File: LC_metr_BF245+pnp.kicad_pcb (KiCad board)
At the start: 2 copper layers, 37 x 33.5 mm, 16 parts, among them J1 Conn_01x01_Socket, J2 Conn_01x01_Socket, J3 Conn_02x01, J4 Conn_01x01_Socket, J5 Conn_01x01_Socket, Q1 MPSA92, Q2 BF245A, U2 LM317_TO-252

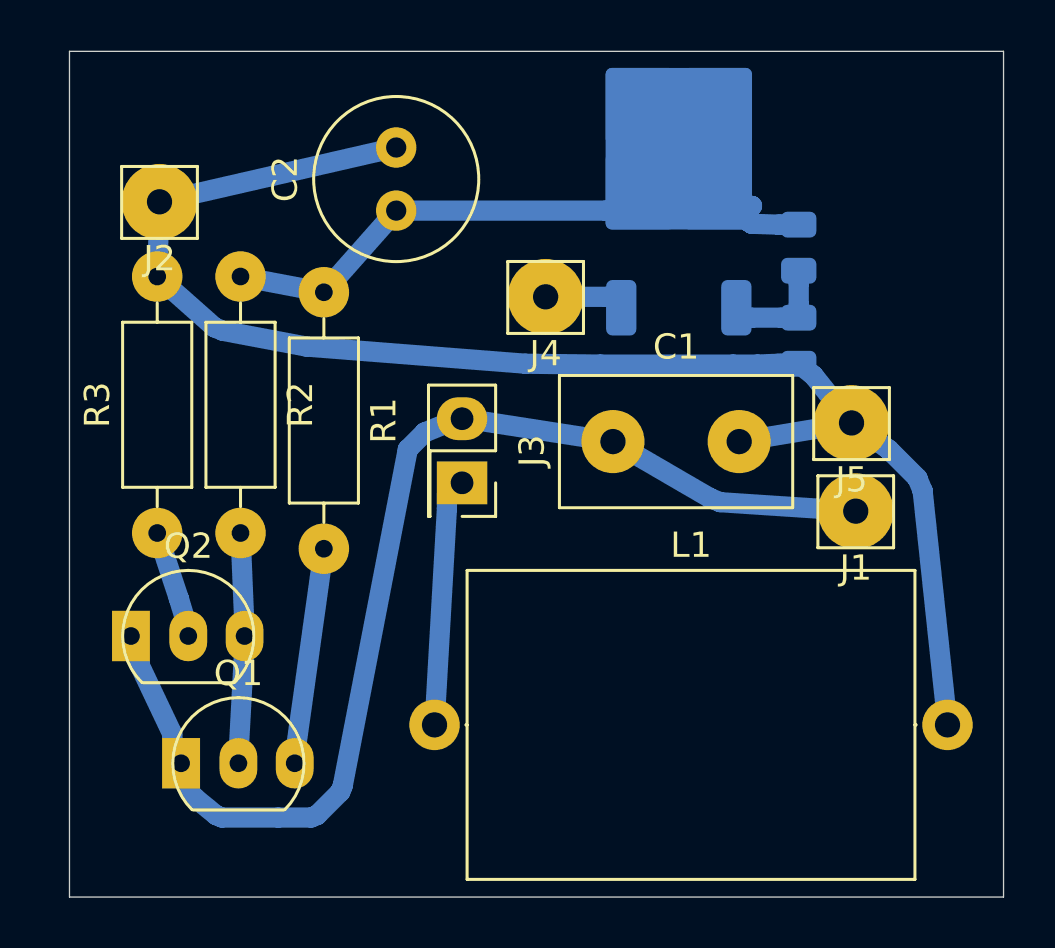
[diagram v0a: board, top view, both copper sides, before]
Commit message: оптимизация и доработка
добавлены выходные клемы, оптимизированно размещение элементов топором
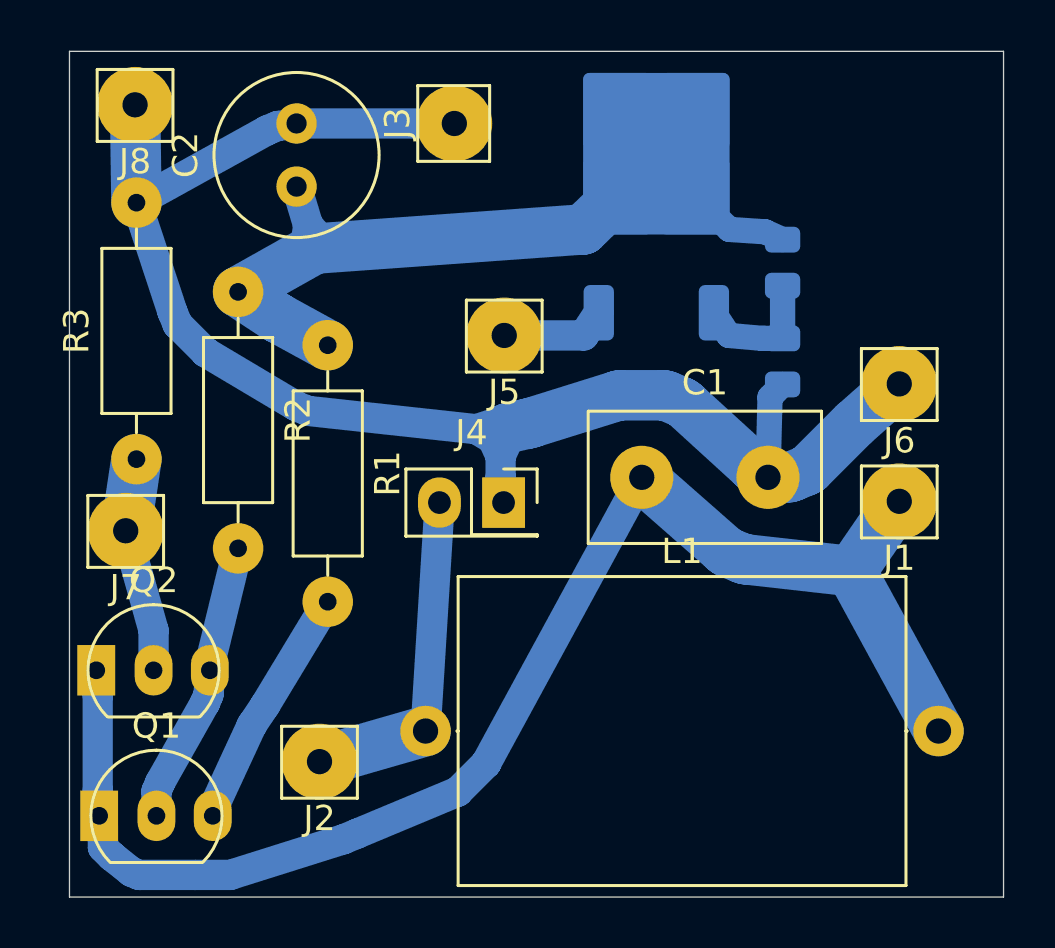
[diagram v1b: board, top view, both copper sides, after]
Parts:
- removed U2: LM317_TO-252, Package_TO_SOT_SMD:TO-252-2
- added J6: Conn_01x01_Socket, main:Pin_3mm_Dril_1mm, F.Cu at (59.9, 37.6)
- added J7: Conn_01x01_Socket, main:Pin_3mm_Dril_1mm, F.Cu at (29.3, 43.4)
- added J8: Conn_01x01_Socket, main:Pin_3mm_Dril_1mm, F.Cu at (29.6, 26.5)
- added U1: LM317_TO-252, Package_TO_SOT_SMD:TO-252-2, B.Cu at (50.3, 29.7)
- J3: value Conn_02x01 -> Conn_01x01_Socket; footprint main:PinSocket_2x01_P2.54mm_Vertical -> main:Pin_3mm_Dril_1mm
- J4: value Conn_01x01_Socket -> Conn_02x01; footprint main:Pin_3mm_Dril_1mm -> main:PinSocket_2x01_P2.54mm_Vertical
- moved J2 23.1 mm to (37.0, 52.5)
- moved J3 14.2 mm to (42.3, 27.2)
- moved J5 14.2 mm to (44.3, 35.6)
- moved J4 8.32 mm to (44.2, 42.3)
- moved C2 4.06 mm to (36.0, 29.8)
- moved Q1 3.86 mm to (29.2, 54.7)
- moved R3 3.04 mm to (29.7, 40.5)
- moved R1 2.10 mm to (37.3, 36.0)
- moved Q2 1.93 mm to (29.1, 48.9)
- moved C1 1.82 mm to (49.7, 41.3)
- moved J1 1.77 mm to (59.9, 42.2)
- moved R5 1.04 mm to (55.3, 36.7)
- moved R4 0.87 mm to (55.3, 32.8)
- moved R2 0.62 mm to (33.7, 33.9)
- moved L1 0.43 mm to (41.2, 51.3)
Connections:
- J2 pad 1: GND -> Net-(J2-Pin_1)
- J3 pad 1: Net-(J3-Pin_1) -> GND
- J4 pad 1: +12V -> GND
- J5 pad 1: GND -> +12V
- L1 pad 1: Net-(J3-Pin_1) -> Net-(J2-Pin_1)
- L1 pad 2: GND -> Net-(J1-Pin_1)
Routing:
- net Net-(J2-Pin_1): track 0.00 -> 13.4 mm
- net Net-(J1-Pin_1): track 46.2 -> 56.6 mm
- net Net-(J3-Pin_1): track 9.90 -> 0.00 mm
- net +5V: track 22.1 -> 28.6 mm
- net GND: track 59.8 -> 65.1 mm
- net Net-(J7-Pin_1): track 4.27 -> 8.55 mm
- net Net-(Q1-B): track 9.13 -> 11.3 mm
- net Net-(Q1-C): track 8.58 -> 9.67 mm
- net +12V: track 3.27 -> 4.23 mm
- net Net-(U1-ADJ): track 4.57 -> 5.30 mm

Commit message: оптимизация
увеличена ширина проводников до 5 мм
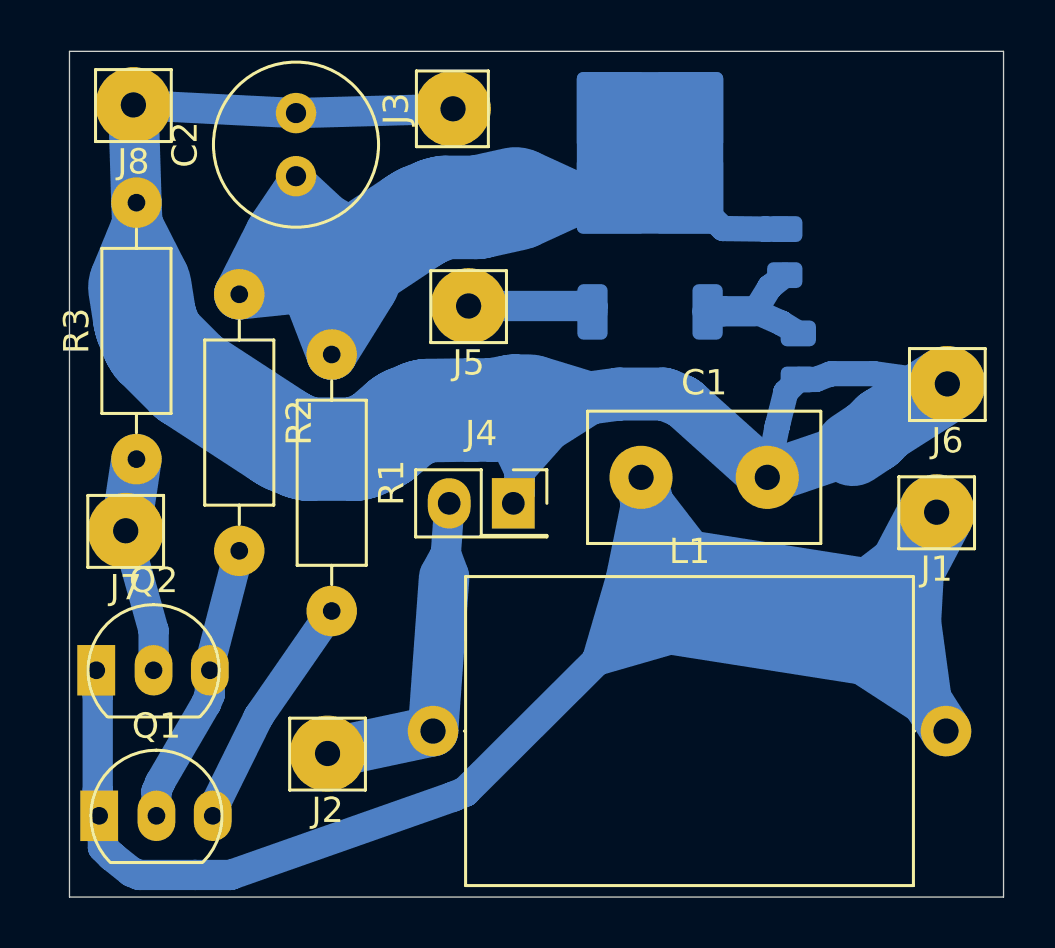
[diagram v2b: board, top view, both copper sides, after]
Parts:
- moved J6 1.91 mm to (61.8, 37.6)
- moved J5 1.83 mm to (42.9, 34.5)
- moved J1 1.54 mm to (61.4, 42.6)
- moved R5 0.65 mm to (55.9, 36.5)
- moved J3 0.58 mm to (42.2, 26.7)
- moved J2 0.45 mm to (37.3, 52.2)
- moved R4 0.43 mm to (55.4, 32.3)
- moved C2 0.41 mm to (36.0, 29.3)
- moved R1 0.40 mm to (37.4, 36.4)
- moved J4 0.39 mm to (44.6, 42.3)
- moved L1 0.30 mm to (41.4, 51.3)
- moved U1 0.25 mm to (50.0, 29.7)
- moved R2 0.11 mm to (33.8, 34.0)
- moved J8 0.07 mm to (29.6, 26.5)
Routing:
- net Net-(J1-Pin_1): track 56.6 -> 80.9 mm
- net GND: track 65.1 -> 85.1 mm
- net +5V: track 28.6 -> 47.3 mm
- net Net-(J2-Pin_1): track 13.4 -> 15.1 mm
- net +12V: track 4.23 -> 5.14 mm

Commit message: полигоны
найден баг с зазорами полигонов, нужно цепян назначит созданный левый класс,
если оставлять Default то берутся зазоры для полигона из класса цепей и не меняются настройками полигона
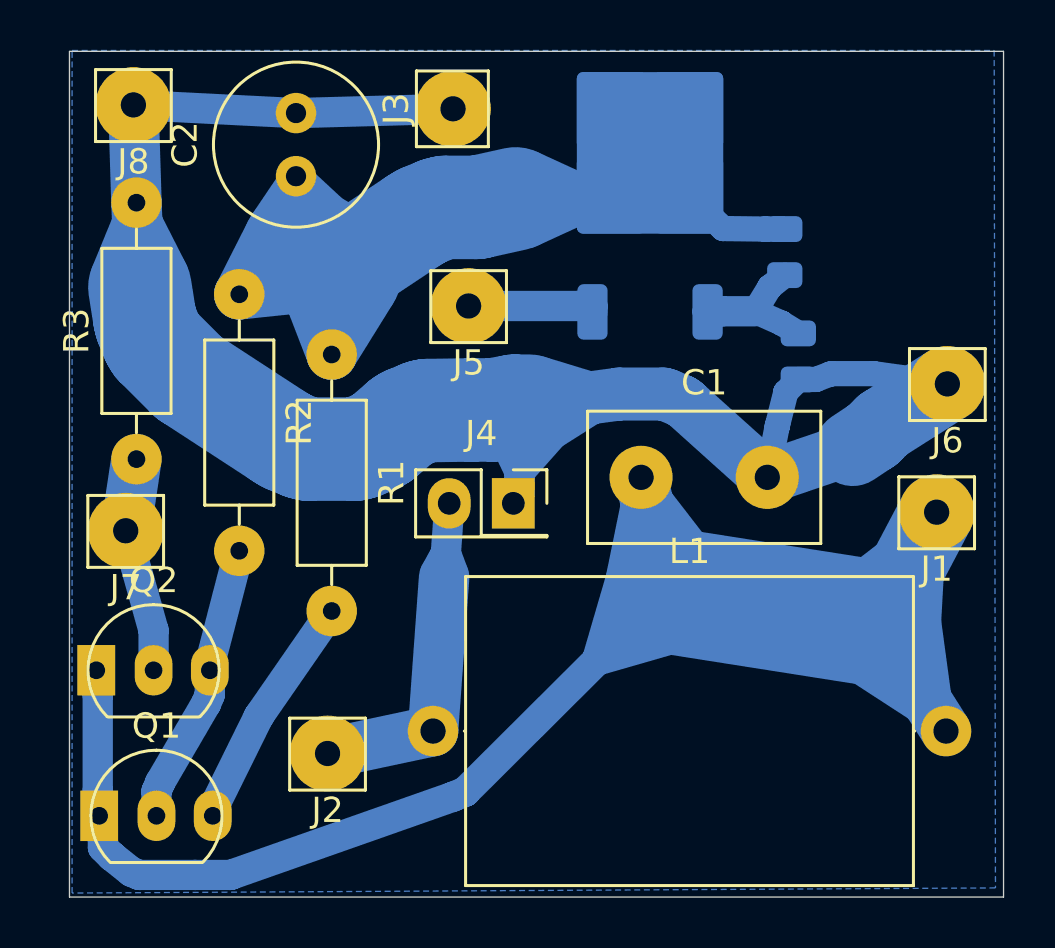
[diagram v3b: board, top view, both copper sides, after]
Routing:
- added copper zone on B.Cu, net GND
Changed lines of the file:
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@@
 		(tenting front back)
 		(pcbplotparams
-			(layerselection 0x00000000_00000000_55555555_55555554)
+			(layerselection 0x00000000_00000000_55555555_55555558)
 			(plot_on_all_layers_selection 0x00000000_00000000_00000000_02000000)
 			(disableapertmacros no)
@@
 			(dxfimperialunits yes)
 			(dxfusepcbnewfont yes)
-			(psnegative yes)
+			(psnegative no)
 			(psa4output no)
 			(plot_black_and_white yes)
@@
 			(outputformat 4)
 			(mirror yes)
-			(drillshape 1)
+			(drillshape 0)
 			(scaleselection 1)
 			(outputdirectory "./")
@@
 		(net 9)
 	)
+	(zone
+		(net 2)
+		(net_name "GND")
+		(layer "B.Cu")
+		(hatch edge 0.5)
+		(connect_pads
+			(clearance 2)
+		)
+		(min_thickness 0.5)
+		(filled_areas_thickness no)
+		(fill yes
+			(thermal_gap 0.5)
+			(thermal_bridge_width 0.5)
+		)
+		(polygon
+			(pts
+				(xy 27.1526 24.3586) (xy 63.6778 24.3586) (xy 63.7286 57.531) (xy 27.1526 57.7342)
+			)
+		)
+	)
 	(embedded_fonts no)
